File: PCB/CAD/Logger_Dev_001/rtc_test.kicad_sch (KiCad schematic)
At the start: 1 part, among them U3 MCP7940N-xMNY

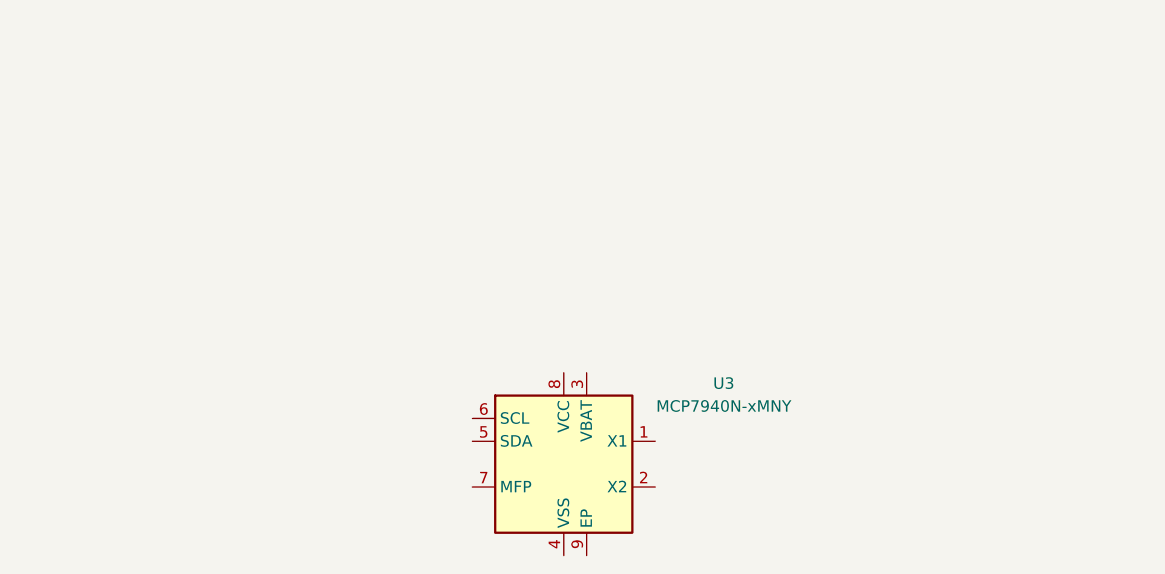
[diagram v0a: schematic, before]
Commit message: JLCPCB Component Updates
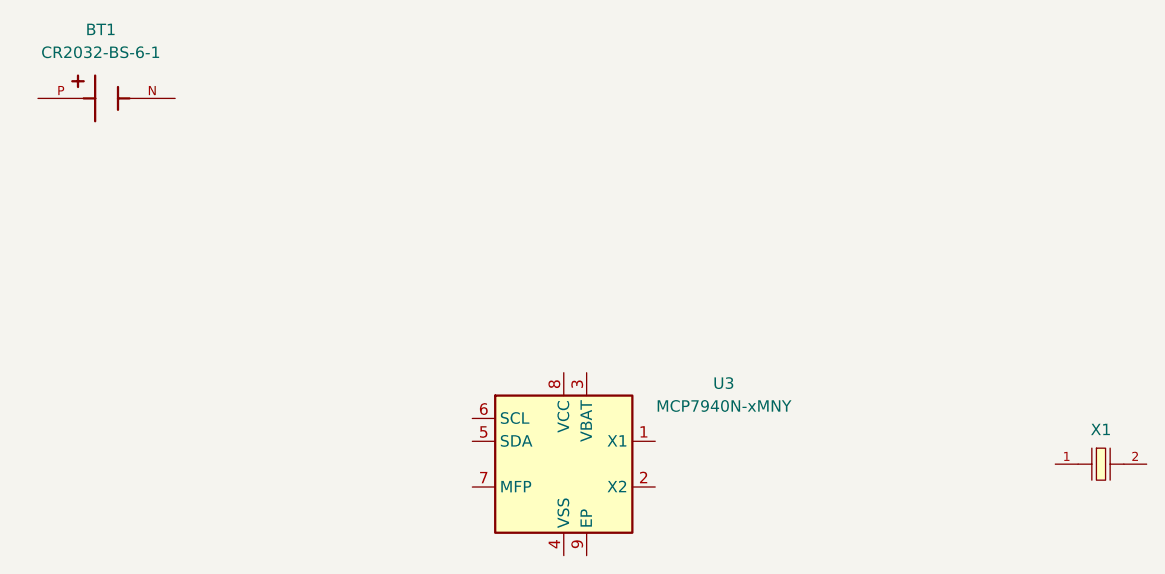
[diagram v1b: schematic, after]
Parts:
- added BT1: CR2032-BS-6-1, CR2032-BS-6-1:BAT_CR2032-BS-6-1, symbol CR2032-BS-6-1:CR2032-BS-6-1
- added X1: Q13FC1350000400, PCM_JLCPCB:FC-135R_L3.2-W1.5, symbol PCM_JLCPCB-Crystals:Crystal, 32.768kHz, 13pF

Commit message: Updated Schematic
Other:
- company: (none) -> Jake Odgers
- title: (none) -> Mileage Logger
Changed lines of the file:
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@@
 	(generator_version "9.0")
 	(paper "A4")
+	(title_block
+		(title "Mileage Logger")
+		(rev "DEV_001")
+		(company "Jake Odgers")
+	)
 	(symbol
 		(lib_id "Timer_RTC:MCP7940N-xMNY")

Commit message: Schematic finalised
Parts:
- removed BT1: CR2032-BS-6-1, CR2032-BS-6-1:BAT_CR2032-BS-6-1, symbol CR2032-BS-6-1:CR2032-BS-6-1
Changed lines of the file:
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@@
-	)
-	(symbol
-		(lib_id "CR2032-BS-6-1:CR2032-BS-6-1")
-		(at 92.71 52.07 0)
-		(unit 1)
-		(exclude_from_sim no)
-		(in_bom yes)
-		(on_board yes)
-		(dnp no)
-		(fields_autoplaced yes)
-		(property "Reference" "BT1"
-			(at 92.075 44.45 0)
-			(effects
-				(font
-					(size 1.27 1.27)
-				)
-			)
-		)
-		(property "Value" "CR2032-BS-6-1"
-			(at 92.075 46.99 0)
-			(effects
-				(font
-					(size 1.27 1.27)
-				)
-			)
-		)
-		(property "Footprint" "CR2032-BS-6-1:BAT_CR2032-BS-6-1"
-			(at 92.71 52.07 0)
-			(effects
-				(font
-					(size 1.27 1.27)
-				)
-				(justify bottom)
-				(hide yes)
-			)
-		)
-		(property "Datasheet" ""
-			(at 92.71 52.07 0)
-			(effects
-				(font
-					(size 1.27 1.27)
-				)
-				(hide yes)
-			)
-		)
-		(property "Description" ""
-			(at 92.71 52.07 0)
-			(effects
-				(font
-					(size 1.27 1.27)
-				)
-				(hide yes)
-			)
-		)
-		(property "MF" "Shenzhen Q&J Electronics Co. Ltd"
-			(at 92.71 52.07 0)
-			(effects
-				(font
-					(size 1.27 1.27)
-				)
-				(justify bottom)
-				(hide yes)
-			)
-		)
-		(property "MAXIMUM_PACKAGE_HEIGHT" "5.55mm"
-			(at 92.71 52.07 0)
-			(effects
-				(font
-					(size 1.27 1.27)
-				)
-				(justify bottom)
-				(hide yes)
-			)
-		)
-		(property "Package" "Package"
-			(at 92.71 52.07 0)
-			(effects
-				(font
-					(size 1.27 1.27)
-				)
-				(justify bottom)
-				(hide yes)
-			)
-		)
-		(property "Price" "None"
-			(at 92.71 52.07 0)
-			(effects
-				(font
-					(size 1.27 1.27)
-				)
-				(justify bottom)
-				(hide yes)
-			)
-		)
-		(property "Check_prices" "https://www.snapeda.com/parts/CR2032-BS-6-1/Shenzhen+Huacan+Tianlu+Electronics+Co.%252C+Ltd./view-part/?ref=eda"
-			(at 92.71 52.07 0)
-			(effects
-				(font
-					(size 1.27 1.27)
-				)
-				(justify bottom)
-				(hide yes)
-			)
-		)
-		(property "STANDARD" "Manufacturer Recommendations"
-			(at 92.71 52.07 0)
-			(effects
-				(font
-					(size 1.27 1.27)
-				)
-				(justify bottom)
-				(hide yes)
-			)
-		)
-		(property "PARTREV" "2011/2/14"
-			(at 92.71 52.07 0)
-			(effects
-				(font
-					(size 1.27 1.27)
-				)
-				(justify bottom)
-				(hide yes)
-			)
-		)
-		(property "SnapEDA_Link" "https://www.snapeda.com/parts/CR2032-BS-6-1/Shenzhen+Huacan+Tianlu+Electronics+Co.%252C+Ltd./view-part/?ref=snap"
-			(at 92.71 52.07 0)
-			(effects
-				(font
-					(size 1.27 1.27)
-				)
-				(justify bottom)
-				(hide yes)
-			)
-		)
-		(property "MP" "CR2032-BS-6-1"
-			(at 92.71 52.07 0)
-			(effects
-				(font
-					(size 1.27 1.27)
-				)
-				(justify bottom)
-				(hide yes)
-			)
-		)
-		(property "Description_1" "Battery base CR2032 SMD Battery Connectors ROHS"
-			(at 92.71 52.07 0)
-			(effects
-				(font
-					(size 1.27 1.27)
-				)
-				(justify bottom)
-				(hide yes)
-			)
-		)
-		(property "SNAPEDA_PN" "CR2032-BS-6-1"
-			(at 92.71 52.07 0)
-			(effects
-				(font
-					(size 1.27 1.27)
-				)
-				(justify bottom)
-				(hide yes)
-			)
-		)
-		(property "Availability" "Not in stock"
-			(at 92.71 52.07 0)
-			(effects
-				(font
-					(size 1.27 1.27)
-				)
-				(justify bottom)
-				(hide yes)
-			)
-		)
-		(property "MANUFACTURER" "Shenzhen Q and J Electronics"
-			(at 92.71 52.07 0)
-			(effects
-				(font
-					(size 1.27 1.27)
-				)
-				(justify bottom)
-				(hide yes)
-			)
-		)
-		(pin "P"
-		)
-		(pin "N"
-		)
-		(instances
-			(project ""
-				(path "/9546b831-c7ee-4f40-8993-5fd5a38d4078/907c050a-0390-4385-90cd-8ef4ffb8a61c"
-					(reference "BT1")
-					(unit 1)
-				)
-			)
-		)
 	)
 	(symbol
